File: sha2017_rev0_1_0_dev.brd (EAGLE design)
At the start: 95 x 86 mm, 194 parts, among them IC1 CP210X_USB_UART, IC2 AP7215, IC3 ESP32WROOM32, IC4 MCP73833, IC5 FXL6408, IC6 CPT112, Q1 MOSFET-PCHANNEL, Q2 MMBT2222A, Q3 MMBT2222A, Q4 MMBT2222A, Q5 MMBT2222A, Q6 SI1304 BDL, Q7 MMBT2222A, Q8 MOSFET-PCHANNEL, Q9 MMBT2222A, T1 SI2301DS, X1 JST-PH3, X2 2908-05WB-MG

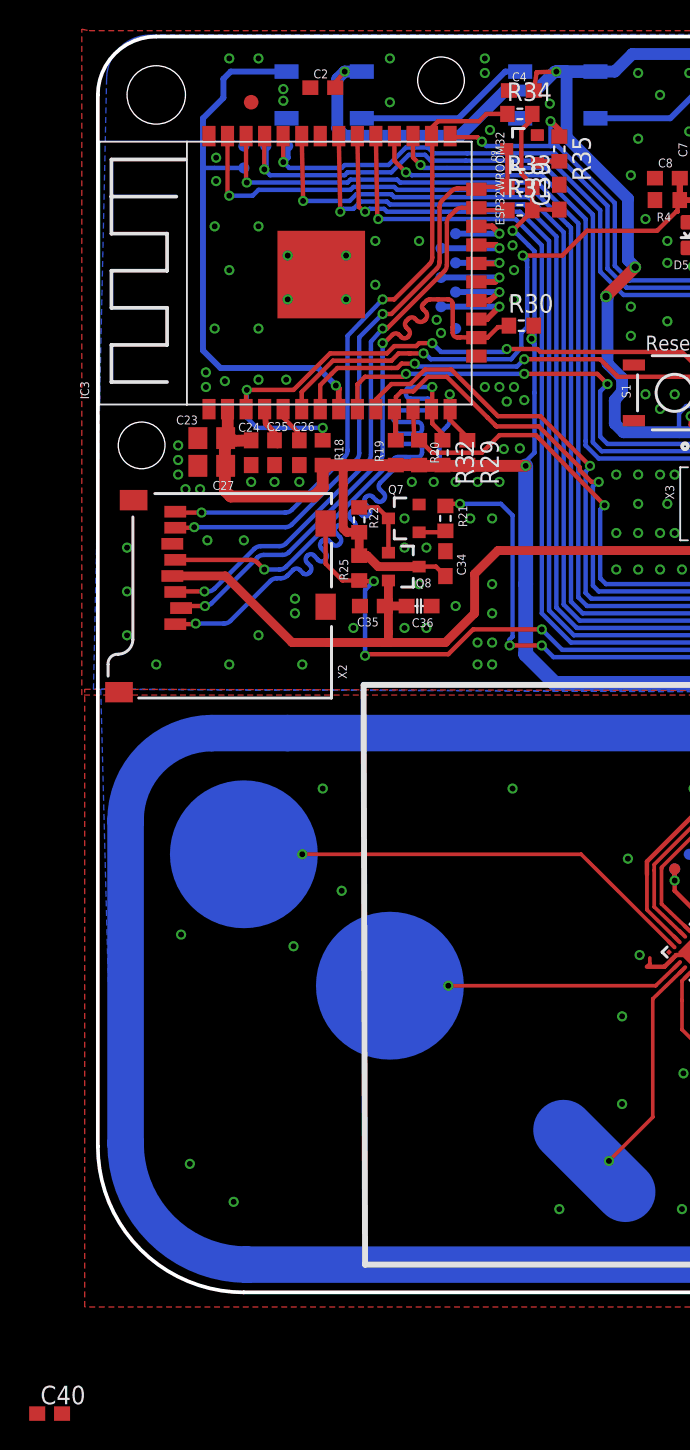
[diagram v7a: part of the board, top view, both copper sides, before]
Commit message: replaced transistor with a diode becaus we need it non inverting
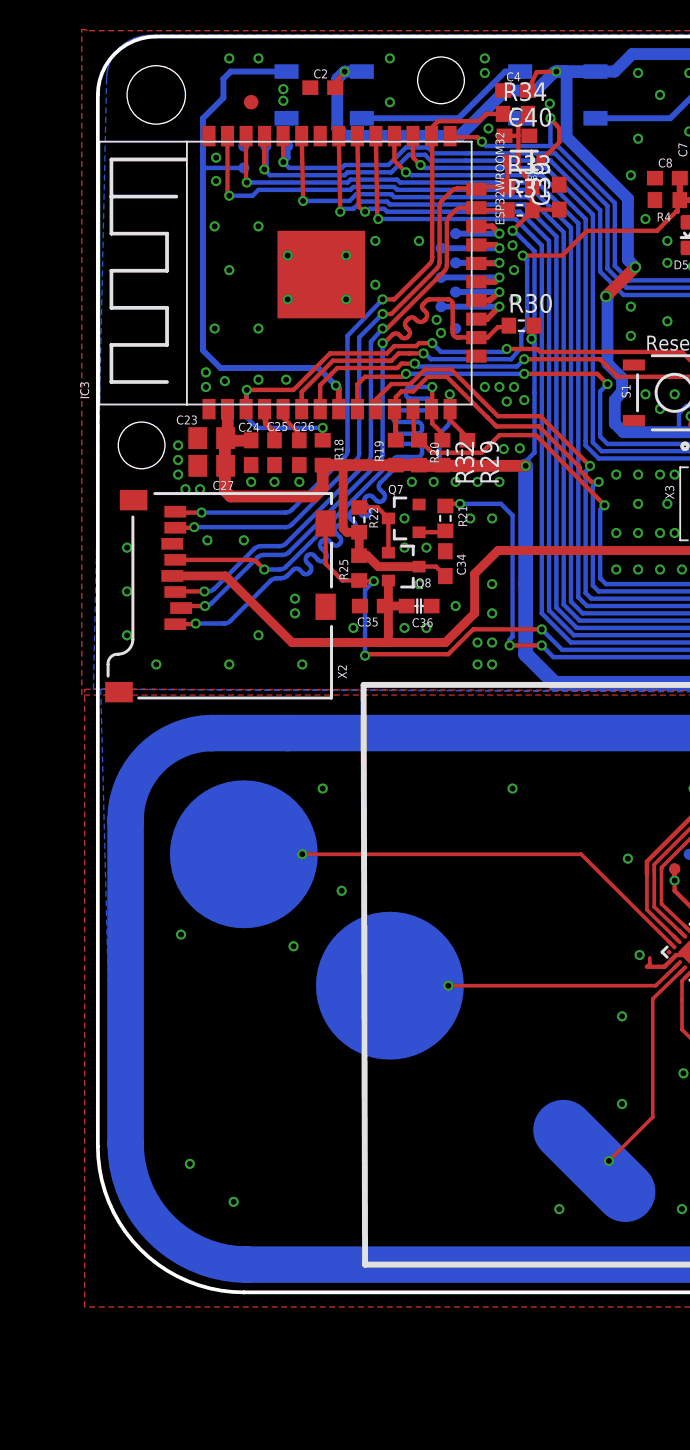
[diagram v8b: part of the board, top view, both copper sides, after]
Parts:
- removed Q9: MMBT2222A, SparkFun-DiscreteSemi:SOT23-3
- removed R35: 10k, 00ralf:R0603-DASHES
- added D9: NSVR0320MW2T1G, SparkFun-DiscreteSemi:SOD-323
- moved C40 93.2 mm to (28.7, 78.2)
- moved C4 0.40 mm to (28.6, 81.3)
- moved R34 0.30 mm to (28.6, 79.7)
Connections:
- removed net N$20: Q9.1, R35.2
- net ESP32_FLASH: now also D9.C; no longer R35.1
- net GND: no longer Q9.2
- net SD_DATA0: now also D9.A; no longer Q9.3
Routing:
- net ESP32_FLASH: track 50.4 -> 52.9 mm
- net N$20: track 1.54 -> 0.00 mm
- net +3V3: track 269.3 -> 270.4 mm
- net SD_DATA0: track 42.2 -> 41.4 mm
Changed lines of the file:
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@@
 <attribute name="VALUE" x="55.705" y="81.265" size="1.27" layer="27" rot="R90"/>
 </element>
-<element name="C4" library="rcl" package="C0603" value="100n" x="29" y="81.3" smashed="yes">
-<attribute name="NAME" x="28.365" y="81.935" size="0.6096" layer="25" font="vector" ratio="16"/>
-<attribute name="VALUE" x="28.365" y="79.395" size="1.27" layer="27"/>
+<element name="C4" library="rcl" package="C0603" value="100n" x="28.6" y="81.3" smashed="yes">
+<attribute name="NAME" x="27.965" y="81.935" size="0.6096" layer="25" font="vector" ratio="16"/>
+<attribute name="VALUE" x="27.965" y="79.395" size="1.27" layer="27"/>
 </element>
 <element name="C2" library="rcl" package="C0603" value="100n" x="15.4" y="81.5" smashed="yes">
@@
 <element name="R32" library="00ralf" package="R0603-DASHES" value="10k" x="23.6" y="56.5" rot="R270"/>
 <element name="R33" library="00ralf" package="R0603-DASHES" value="10k" x="28.9" y="74.7"/>
-<element name="R34" library="00ralf" package="R0603-DASHES" value="10k" x="28.9" y="79.7"/>
-<element name="Q9" library="SparkFun-DiscreteSemi" package="SOT23-3" value="MMBT2222A" x="29.1" y="77.3" rot="R90">
-<attribute name="PROD_ID" value="TRANS-08049" x="29.1" y="77.3" size="1.778" layer="27" rot="R90" display="off"/>
-</element>
-<element name="R35" library="00ralf" package="R0603-DASHES" value="10k" x="31.6" y="77.3" rot="R270"/>
+<element name="R34" library="00ralf" package="R0603-DASHES" value="10k" x="28.6" y="79.7"/>
 <element name="C39" library="rcl" package="C0603" value="100n" x="31.6" y="74" rot="R90">
 <attribute name="PARTNO" value="GRM188R71H104KA93D" x="31.6" y="74" size="1.778" layer="27" rot="R90" display="off"/>
 </element>
-<element name="C40" library="rcl" package="C0603" value="100n" x="-3.3" y="-9.3">
-<attribute name="PARTNO" value="GRM188R71H104KA93D" x="-3.3" y="-9.3" size="1.778" layer="27" display="off"/>
+<element name="C40" library="rcl" package="C0603" value="100n" x="28.7" y="78.2">
+<attribute name="PARTNO" value="GRM188R71H104KA93D" x="28.7" y="78.2" size="1.778" layer="27" display="off"/>
+</element>
+<element name="D9" library="SparkFun-DiscreteSemi" package="SOD-323" value="NSVR0320MW2T1G" x="29.2" y="76.5" rot="R180">
+<attribute name="PARTNO" value="BAT20JFILM" x="29.2" y="76.5" size="1.778" layer="27" rot="R180" display="off"/>
+<attribute name="PROD_ID" value="DIO-11623" x="29.2" y="76.5" size="1.778" layer="27" rot="R180" display="off"/>
 </element>
 </elements>
@@
 <via x="54.25" y="77.25" extent="1-16" drill="0.4"/>
 <via x="54.25" y="76.25" extent="1-16" drill="0.4"/>
-<via x="26.85" y="78.6" extent="1-16" drill="0.4"/>
+<via x="26.75" y="78.7" extent="1-16" drill="0.4"/>
 <via x="69.5" y="77.5" extent="1-16" drill="0.4"/>
 <via x="8" y="72" extent="1-16" drill="0.4"/>
@@
 <via x="8.1" y="76.7" extent="1-16" drill="0.4"/>
 <via x="8.1" y="75.1" extent="1-16" drill="0.4"/>
-<contactref element="Q9" pad="2"/>
 <via x="7.4" y="62" extent="1-16" drill="0.4"/>
 <via x="7.4" y="61" extent="1-16" drill="0.4"/>
@@
 <contactref element="C40" pad="2"/>
 <via x="30.95" y="80.4" extent="1-16" drill="0.4"/>
-<wire x1="9.3" y1="5.2" x2="-2.45" y2="-9.3" width="0" layer="19" extent="1-1"/>
 </signal>
 <signal name="USB_DN_CON">
@@
 <contactref element="R34" pad="2"/>
 <wire x1="29.75" y1="74.7" x2="29.75" y2="74.85" width="0.3048" layer="1"/>
-<wire x1="29.75" y1="74.85" x2="29" y2="75.6" width="0.3048" layer="1"/>
-<wire x1="29" y1="75.6" x2="29" y2="78.6" width="0.3048" layer="1"/>
-<wire x1="29" y1="78.6" x2="29.6" y2="79.2" width="0.3048" layer="1"/>
-<wire x1="29.6" y1="79.2" x2="29.6" y2="79.55" width="0.3048" layer="1"/>
-<wire x1="29.6" y1="79.55" x2="29.75" y2="79.7" width="0.3048" layer="1"/>
+<wire x1="29.75" y1="74.85" x2="28.8" y2="76" width="0.3048" layer="1"/>
+<wire x1="28.8" y1="76" x2="28.8" y2="78.2" width="0.3048" layer="1"/>
+<wire x1="28.8" y1="78.2" x2="28.8" y2="78.9" width="0.3048" layer="1"/>
+<wire x1="28.8" y1="78.9" x2="29.3" y2="79.4" width="0.3048" layer="1"/>
+<wire x1="29.3" y1="79.4" x2="29.6" y2="79.55" width="0.3048" layer="1"/>
+<wire x1="29.6" y1="79.55" x2="29.45" y2="79.7" width="0.3048" layer="1"/>
 <contactref element="C40" pad="1"/>
 <contactref element="C39" pad="1"/>
@@
 <wire x1="28.4" y1="71.7" x2="29.75" y2="73.05" width="0.3048" layer="1"/>
 <wire x1="29.75" y1="73.05" x2="29.75" y2="73.1" width="0.3048" layer="1"/>
-<wire x1="-4.15" y1="-9.3" x2="41.80455" y2="23.55810625" width="0" layer="19" extent="1-1"/>
+<wire x1="27.85" y1="78.2" x2="28.8" y2="78.2" width="0.3048" layer="1"/>
 </signal>
 <signal name="GDR">
@@
 <wire x1="23.2140125" y1="69.1140125" x2="20.1" y2="66" width="0.3048" layer="1"/>
 <contactref element="R33" pad="1"/>
-<contactref element="Q9" pad="3"/>
 <wire x1="28.05" y1="74.7" x2="26.08" y2="74.7" width="0.3048" layer="1"/>
 <wire x1="26.08" y1="74.7" x2="25.92" y2="74.54" width="0.3048" layer="1"/>
-<wire x1="28.05" y1="74.7" x2="28.05" y2="77.25" width="0.3048" layer="1"/>
-<wire x1="28.05" y1="77.25" x2="28" y2="77.3" width="0.3048" layer="1"/>
+<contactref element="D9" pad="A"/>
+<wire x1="28.05" y1="74.7" x2="28.05" y2="76.5" width="0.3048" layer="1"/>
 </signal>
 <signal name="SD_DATA1">
@@
 <wire x1="23.3" y1="79.2" x2="26.1" y2="79.2" width="0.3048" layer="1"/>
 <wire x1="26.1" y1="79.2" x2="26.6" y2="79.7" width="0.3048" layer="1"/>
-<wire x1="26.6" y1="79.7" x2="28.05" y2="79.7" width="0.3048" layer="1"/>
+<wire x1="26.6" y1="79.7" x2="27.75" y2="79.7" width="0.3048" layer="1"/>
 </signal>
 <signal name="SD_DATA3">
@@
 <via x="52.4" y="82.6" extent="1-16" drill="0.4"/>
 <wire x1="52.4" y1="82.6" x2="51.8" y2="82.6" width="0.3048" layer="16"/>
-<wire x1="29.85" y1="81.3" x2="30.05" y2="82.55" width="0.3048" layer="1"/>
+<wire x1="29.45" y1="81.3" x2="30.05" y2="82.55" width="0.3048" layer="1"/>
 <wire x1="30.05" y1="82.55" x2="31.4" y2="82.6" width="0.3048" layer="1"/>
 <via x="31.4" y="82.6" extent="1-16" drill="0.4"/>
@@
 <via x="47.5" y="62.5" extent="1-16" drill="0.4"/>
 <wire x1="47.5" y1="62.5" x2="50.394" y2="62.505" width="0.3048" layer="1"/>
-<contactref element="R35" pad="1"/>
-<wire x1="31.6" y1="78.15" x2="31.6" y2="78.6" width="0.4064" layer="1"/>
-<wire x1="31.6" y1="78.6" x2="31" y2="79.2" width="0.4064" layer="1"/>
-<via x="31" y="79.2" extent="1-16" drill="0.4"/>
-<wire x1="31" y1="79.2" x2="31" y2="77.5" width="0.3048" layer="16"/>
-</signal>
-<signal name="N$20">
-<contactref element="Q9" pad="1"/>
-<contactref element="R35" pad="2"/>
-<wire x1="31.6" y1="76.45" x2="30.2" y2="76.45" width="0.3048" layer="1"/>
-<wire x1="30.2" y1="76.45" x2="30.1" y2="76.35" width="0.3048" layer="1"/>
+<wire x1="31.6" y1="78.7" x2="31" y2="79.4" width="0.3048" layer="1"/>
+<via x="31" y="79.4" extent="1-16" drill="0.4"/>
+<wire x1="31" y1="79.4" x2="31" y2="77.5" width="0.3048" layer="16"/>
+<contactref element="D9" pad="C"/>
+<wire x1="30.35" y1="76.5" x2="31.6" y2="77.75" width="0.3048" layer="1"/>
+<wire x1="31.6" y1="77.75" x2="31.6" y2="78.7" width="0.3048" layer="1"/>
 </signal>
 </signals>
